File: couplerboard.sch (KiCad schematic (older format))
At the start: 15 parts, among them J1 X, J2 Y, J3 Z, J4 Conn_01x05, U1 LTV-817, U2 LTV-817, U3 LTV-817

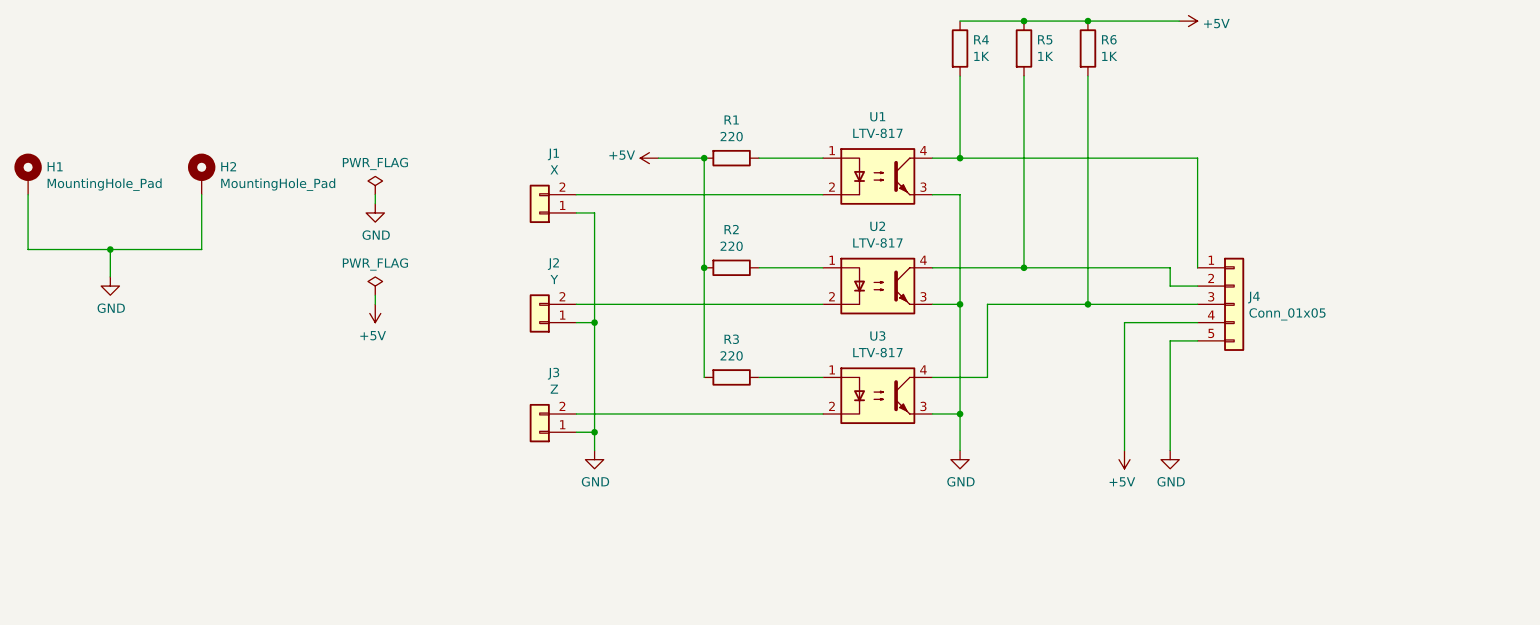
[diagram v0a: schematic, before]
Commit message: Added mono jack for probe
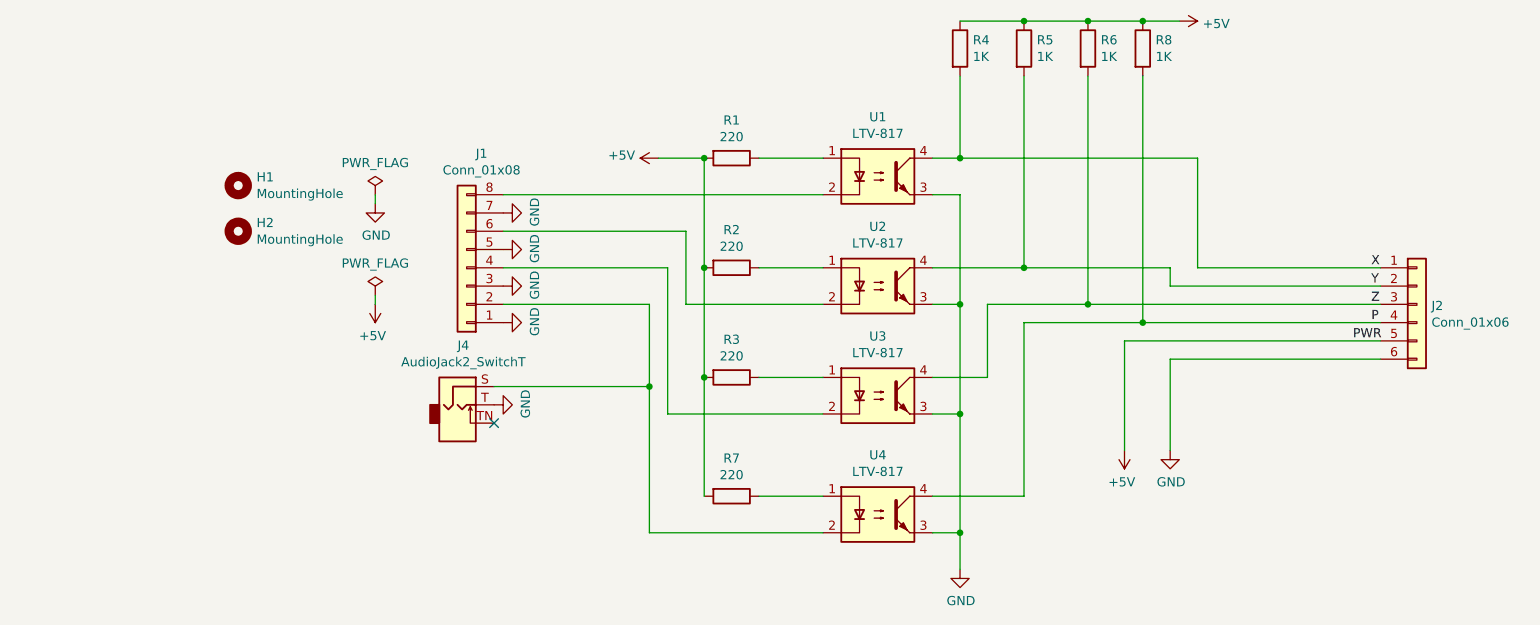
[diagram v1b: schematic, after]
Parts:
- removed H1, H2: MountingHole_Pad, MountingHole:MountingHole_3.2mm_M3_DIN965_Pad, symbol Mechanical:MountingHole_Pad
- removed J1: X, TerminalBlock_MetzConnect:TerminalBlock_MetzConnect_Type094_RT03502HBLU_1x02_P5.00mm_Horizontal, symbol Connector_Generic:Conn_01x02
- removed J2: Y, TerminalBlock_MetzConnect:TerminalBlock_MetzConnect_Type094_RT03502HBLU_1x02_P5.00mm_Horizontal, symbol Connector_Generic:Conn_01x02
- removed J3: Z, TerminalBlock_MetzConnect:TerminalBlock_MetzConnect_Type094_RT03502HBLU_1x02_P5.00mm_Horizontal, symbol Connector_Generic:Conn_01x02
- removed J4: Conn_01x05, TerminalBlock_MetzConnect:TerminalBlock_MetzConnect_Type094_RT03505HBLU_1x05_P5.00mm_Horizontal, symbol Connector_Generic:Conn_01x05
- added H1, H2: MountingHole, MountingHole:MountingHole_3.2mm_M3_DIN965, symbol Mechanical:MountingHole
- added J1: Conn_01x08, TerminalBlock_MetzConnect:TerminalBlock_MetzConnect_Type094_RT03506HBLU_1x08_P5.00mm_Horizontal, symbol Connector_Generic:Conn_01x08
- added J2: Conn_01x06, TerminalBlock_MetzConnect:TerminalBlock_MetzConnect_Type094_RT03506HBLU_1x06_P5.00mm_Horizontal, symbol Connector_Generic:Conn_01x06
- added J4: AudioJack2_SwitchT, Eurorack:ThonkIcon, symbol Connector:AudioJack2_SwitchT
- added R7: 220, Resistor_THT:R_Axial_DIN0207_L6.3mm_D2.5mm_P7.62mm_Horizontal, symbol Device:R
- added R8: 1K, Resistor_THT:R_Axial_DIN0207_L6.3mm_D2.5mm_P7.62mm_Horizontal, symbol Device:R
- added U4: LTV-817, Package_DIP:DIP-4_W7.62mm, symbol Isolator:LTV-817
- R1, R2, R3, R4, R5, R6: footprint Resistor_THT:R_Axial_DIN0204_L3.6mm_D1.6mm_P5.08mm_Horizontal -> Resistor_THT:R_Axial_DIN0207_L6.3mm_D2.5mm_P7.62mm_Horizontal
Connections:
- net +5V: now also J2.5 (Pin_5), R7.2, R8.1
- net GND: now also J1.1 (Pin_1), J1.3 (Pin_3), J1.5 (Pin_5), J1.7 (Pin_7), J2.6 (Pin_6), J4.T, U4.3
- net X: now reaches R4.2, U1.4
- net X: now also J2.1 (Pin_1)
- net Y: now reaches R5.2, U2.4
- net Y: now also J2.2 (Pin_2)
- net Z: now reaches R6.2, U3.4
- net Z: now also J2.3 (Pin_3)
- net at U1.2: now also J1.8 (Pin_8)
- net at U2.2: now also J1.6 (Pin_6)
- net at U3.2: now also J1.4 (Pin_4)
- new net: R7.1, U4.1
- new net: J1.2 (Pin_2), J4.S, U4.2
- new net P: J2.4 (Pin_4), R8.2, U4.4
- no-connect marks 0 -> 1

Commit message: WIP
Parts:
- added H3, H4: MountingHole, MountingHole:MountingHole_3.2mm_M3_DIN965, symbol Mechanical:MountingHole
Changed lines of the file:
@@
 	4950 4150 4950 3700
 NoConn ~ 4100 4350
+$Comp
+L Mechanical:MountingHole H3
+U 1 1 5EBFE181
+P 2700 3550
+F 0 "H3" H 2800 3596 50  0000 L CNN
+F 1 "MountingHole" H 2800 3505 50  0000 L CNN
+F 2 "MountingHole:MountingHole_3.2mm_M3_DIN965" H 2700 3550 50  0001 C CNN
+F 3 "~" H 2700 3550 50  0001 C CNN
+	1    2700 3550
+	1    0    0    -1
+$EndComp
+$Comp
+L Mechanical:MountingHole H4
+U 1 1 5EBFE53F
+P 2700 3800
+F 0 "H4" H 2800 3846 50  0000 L CNN
+F 1 "MountingHole" H 2800 3755 50  0000 L CNN
+F 2 "MountingHole:MountingHole_3.2mm_M3_DIN965" H 2700 3800 50  0001 C CNN
+F 3 "~" H 2700 3800 50  0001 C CNN
+	1    2700 3800
+	1    0    0    -1
+$EndComp
 $EndSCHEMATC

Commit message: Reannotate
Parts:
- renumbered J4 to J1, J1 to J2, J2 to J3, R7 to R4, R4 to R5, R5 to R6, R6 to R7
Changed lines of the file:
@@
 	6800 4100 6500 4100
 $Comp
-L Device:R R4
+L Device:R R5
 U 1 1 5EB1CD65
 P 6650 2300
-F 0 "R4" H 6720 2346 50  0000 L CNN
+F 0 "R5" H 6720 2346 50  0000 L CNN
 F 1 "1K" H 6720 2255 50  0000 L CNN
 F 2 "Resistor_THT:R_Axial_DIN0207_L6.3mm_D2.5mm_P7.62mm_Horizontal" V 6580 2300 50  0001 C CNN
@@
 $EndComp
 $Comp
-L Device:R R5
+L Device:R R6
 U 1 1 5EB1CDA9
 P 7000 2300
-F 0 "R5" H 7070 2346 50  0000 L CNN
+F 0 "R6" H 7070 2346 50  0000 L CNN
 F 1 "1K" H 7070 2255 50  0000 L CNN
 F 2 "Resistor_THT:R_Axial_DIN0207_L6.3mm_D2.5mm_P7.62mm_Horizontal" V 6930 2300 50  0001 C CNN
@@
 $EndComp
 $Comp
-L Device:R R6
+L Device:R R7
 U 1 1 5EB1CE0F
 P 7350 2300
-F 0 "R6" H 7420 2346 50  0000 L CNN
+F 0 "R7" H 7420 2346 50  0000 L CNN
 F 1 "1K" H 7420 2255 50  0000 L CNN
 F 2 "Resistor_THT:R_Axial_DIN0207_L6.3mm_D2.5mm_P7.62mm_Horizontal" V 7280 2300 50  0001 C CNN
@@
 	7000 2150 7350 2150
 $Comp
-L power:+5V #PWR0103
+L power:+5V #PWR012
 U 1 1 5EB1D516
 P 7850 2150
-F 0 "#PWR0103" H 7850 2000 50  0001 C CNN
+F 0 "#PWR012" H 7850 2000 50  0001 C CNN
 F 1 "+5V" V 7865 2278 50  0000 L CNN
 F 2 "" H 7850 2150 50  0001 C CNN
@@
 	5900 4100 5550 4100
 $Comp
-L power:+5V #PWR0105
+L power:+5V #PWR08
 U 1 1 5EB269ED
 P 5000 2900
-F 0 "#PWR0105" H 5000 2750 50  0001 C CNN
+F 0 "#PWR08" H 5000 2750 50  0001 C CNN
 F 1 "+5V" V 5015 3028 50  0000 L CNN
 F 2 "" H 5000 2900 50  0001 C CNN
@@
 Connection ~ 5250 3500
 $Comp
-L power:GND #PWR0106
+L power:GND #PWR09
 U 1 1 5EB2811C
 P 6650 5150
-F 0 "#PWR0106" H 6650 4900 50  0001 C CNN
+F 0 "#PWR09" H 6650 4900 50  0001 C CNN
 F 1 "GND" H 6655 4977 50  0000 C CNN
 F 2 "" H 6650 5150 50  0001 C CNN
@@
 Connection ~ 5250 2900
 $Comp
-L power:GND #PWR0101
+L power:GND #PWR011
 U 1 1 5EB3932F
 P 7800 4500
-F 0 "#PWR0101" H 7800 4250 50  0001 C CNN
+F 0 "#PWR011" H 7800 4250 50  0001 C CNN
 F 1 "GND" H 7805 4327 50  0000 C CNN
 F 2 "" H 7800 4500 50  0001 C CNN
@@
 	7800 4000 7800 4500
 $Comp
-L power:+5V #PWR0102
+L power:+5V #PWR010
 U 1 1 5EB3CDC5
 P 7550 4500
-F 0 "#PWR0102" H 7550 4350 50  0001 C CNN
+F 0 "#PWR010" H 7550 4350 50  0001 C CNN
 F 1 "+5V" H 7565 4673 50  0000 C CNN
 F 2 "" H 7550 4500 50  0001 C CNN
@@
 	7550 3900 7550 4500
 $Comp
-L power:PWR_FLAG #FLG0101
+L power:PWR_FLAG #FLG02
 U 1 1 5EB3D77A
 P 3450 3650
-F 0 "#FLG0101" H 3450 3725 50  0001 C CNN
+F 0 "#FLG02" H 3450 3725 50  0001 C CNN
 F 1 "PWR_FLAG" H 3450 3824 50  0000 C CNN
 F 2 "" H 3450 3650 50  0001 C CNN
@@
 $EndComp
 $Comp
-L power:PWR_FLAG #FLG0102
+L power:PWR_FLAG #FLG01
 U 1 1 5EB3D7CA
 P 3450 3100
-F 0 "#FLG0102" H 3450 3175 50  0001 C CNN
+F 0 "#FLG01" H 3450 3175 50  0001 C CNN
 F 1 "PWR_FLAG" H 3450 3274 50  0000 C CNN
 F 2 "" H 3450 3100 50  0001 C CNN
@@
 $EndComp
 $Comp
-L power:GND #PWR0107
+L power:GND #PWR01
 U 1 1 5EB3D821
 P 3450 3150
-F 0 "#PWR0107" H 3450 2900 50  0001 C CNN
+F 0 "#PWR01" H 3450 2900 50  0001 C CNN
 F 1 "GND" H 3455 2977 50  0000 C CNN
 F 2 "" H 3450 3150 50  0001 C CNN
@@
 $EndComp
 $Comp
-L power:+5V #PWR0108
+L power:+5V #PWR02
 U 1 1 5EB3E0DC
 P 3450 3700
-F 0 "#PWR0108" H 3450 3550 50  0001 C CNN
+F 0 "#PWR02" H 3450 3550 50  0001 C CNN
 F 1 "+5V" H 3465 3873 50  0000 C CNN
 F 2 "" H 3450 3700 50  0001 C CNN
@@
 $EndComp
 $Comp
-L Device:R R7
+L Device:R R4
 U 1 1 5EBD142E
 P 5400 4750
-F 0 "R7" V 5193 4750 50  0000 C CNN
+F 0 "R4" V 5193 4750 50  0000 C CNN
 F 1 "220" V 5284 4750 50  0000 C CNN
 F 2 "Resistor_THT:R_Axial_DIN0207_L6.3mm_D2.5mm_P7.62mm_Horizontal" V 5330 4750 50  0001 C CNN
@@
 	5550 4750 5900 4750
 $Comp
-L Connector_Generic:Conn_01x08 J1
+L Connector_Generic:Conn_01x08 J2
 U 1 1 5EBD529E
 P 3950 3500
-F 0 "J1" H 3868 2875 50  0000 C CNN
+F 0 "J2" H 3868 2875 50  0000 C CNN
 F 1 "Conn_01x08" H 3868 2966 50  0000 C CNN
 F 2 "TerminalBlock_MetzConnect:TerminalBlock_MetzConnect_Type094_RT03506HBLU_1x08_P5.00mm_Horizontal" H 3950 3500 50  0001 C CNN
@@
 $EndComp
 $Comp
-L Connector_Generic:Conn_01x06 J2
+L Connector_Generic:Conn_01x06 J3
 U 1 1 5EBD820A
 P 9150 3700
-F 0 "J2" H 9230 3692 50  0000 L CNN
+F 0 "J3" H 9230 3692 50  0000 L CNN
 F 1 "Conn_01x06" H 9230 3601 50  0000 L CNN
 F 2 "TerminalBlock_MetzConnect:TerminalBlock_MetzConnect_Type094_RT03506HBLU_1x06_P5.00mm_Horizontal" H 9150 3700 50  0001 C CNN
@@
 	4950 3700 4150 3700
 $Comp
-L power:GND #PWR0104
+L power:GND #PWR04
 U 1 1 5EBF3AF0
 P 4150 3200
-F 0 "#PWR0104" H 4150 2950 50  0001 C CNN
+F 0 "#PWR04" H 4150 2950 50  0001 C CNN
 F 1 "GND" H 4155 3027 50  0000 C CNN
 F 2 "" H 4150 3200 50  0001 C CNN
@@
 $EndComp
 $Comp
-L power:GND #PWR0109
+L power:GND #PWR05
 U 1 1 5EBF44DD
 P 4150 3400
-F 0 "#PWR0109" H 4150 3150 50  0001 C CNN
+F 0 "#PWR05" H 4150 3150 50  0001 C CNN
 F 1 "GND" H 4155 3227 50  0000 C CNN
 F 2 "" H 4150 3400 50  0001 C CNN
@@
 $EndComp
 $Comp
-L power:GND #PWR0110
+L power:GND #PWR06
 U 1 1 5EBF46C5
 P 4150 3600
-F 0 "#PWR0110" H 4150 3350 50  0001 C CNN
+F 0 "#PWR06" H 4150 3350 50  0001 C CNN
 F 1 "GND" H 4155 3427 50  0000 C CNN
 F 2 "" H 4150 3600 50  0001 C CNN
@@
 $EndComp
 $Comp
-L power:GND #PWR0111
+L power:GND #PWR07
 U 1 1 5EBF4913
 P 4150 3800
-F 0 "#PWR0111" H 4150 3550 50  0001 C CNN
+F 0 "#PWR07" H 4150 3550 50  0001 C CNN
 F 1 "GND" H 4155 3627 50  0000 C CNN
 F 2 "" H 4150 3800 50  0001 C CNN
@@
 	7650 3800 7000 3800
 $Comp
-L Connector:AudioJack2_SwitchT J4
+L Connector:AudioJack2_SwitchT J1
 U 1 1 5EBE8A51
 P 3900 4250
-F 0 "J4" H 3932 4575 50  0000 C CNN
+F 0 "J1" H 3932 4575 50  0000 C CNN
 F 1 "AudioJack2_SwitchT" H 3932 4484 50  0000 C CNN
 F 2 "Eurorack:ThonkIcon" H 3900 4250 50  0001 C CNN
@@
 $EndComp
 $Comp
-L power:GND #PWR0112
+L power:GND #PWR03
 U 1 1 5EBED915
 P 4100 4250
-F 0 "#PWR0112" H 4100 4000 50  0001 C CNN
+F 0 "#PWR03" H 4100 4000 50  0001 C CNN
 F 1 "GND" H 4105 4077 50  0000 C CNN
 F 2 "" H 4100 4250 50  0001 C CNN
